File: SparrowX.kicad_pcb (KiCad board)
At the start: 4 copper layers, 31.6 x 26.6 mm, 31 parts, among them J1 NORTH, J2 SOUTH, J3 WEST, J4 EAST, U1 LMR43610MSC3RPERQ1, U2 LD49100PU33RY, U3 STM32G0B1CBU6, U4 TCAN332G, U5 TCAN332G

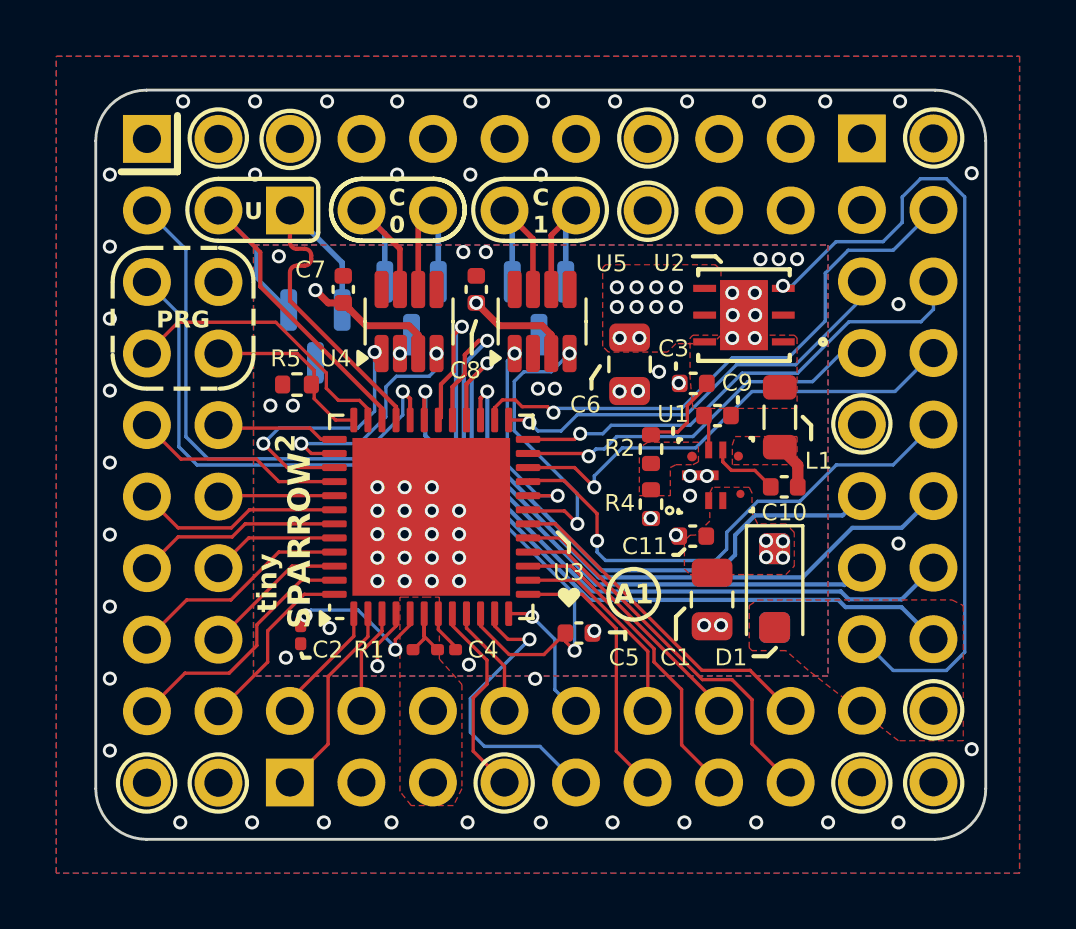
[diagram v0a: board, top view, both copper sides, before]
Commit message: DFM: get rid of 0201 SMD components
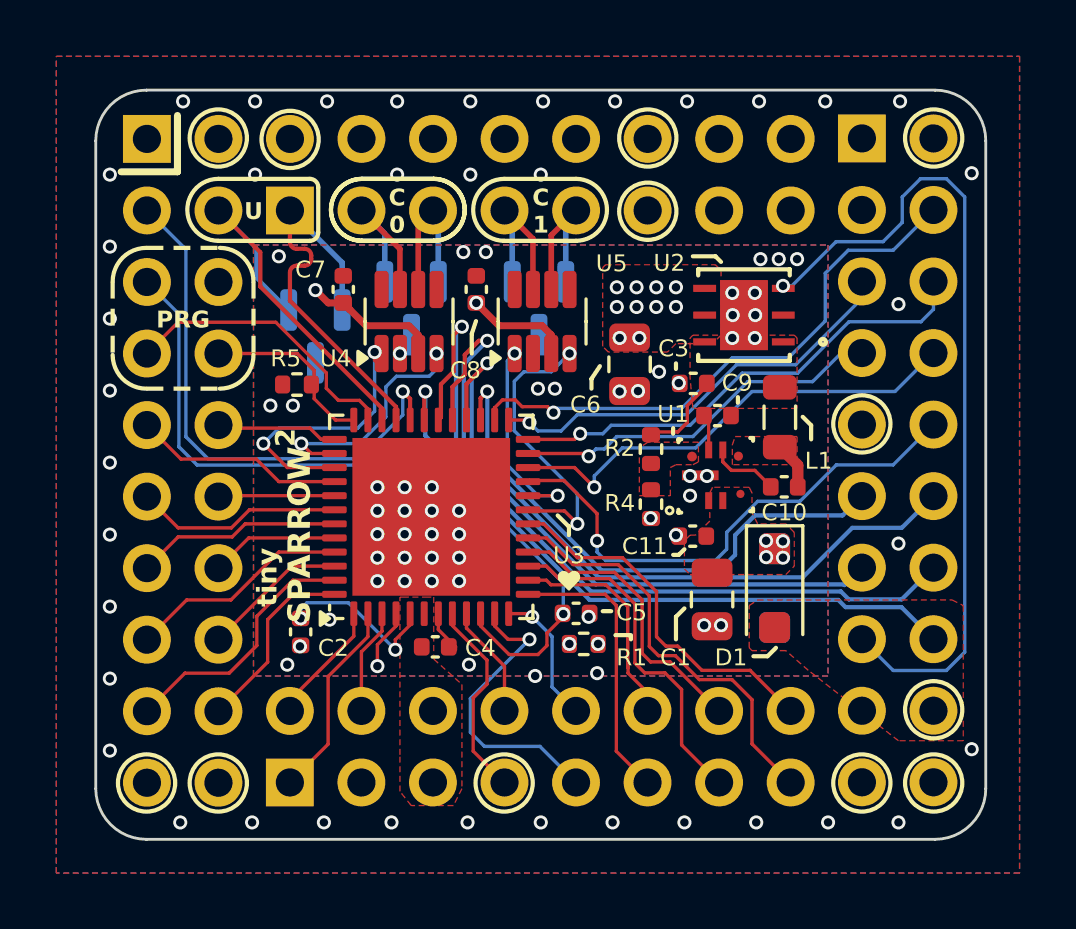
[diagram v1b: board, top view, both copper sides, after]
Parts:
- C1: value 4.7 uF -> 10 uF
- C2, C4: footprint Capacitor_SMD:C_0201_0603Metric -> Capacitor_SMD:C_0402_1005Metric
- R1: footprint Resistor_SMD:R_0201_0603Metric -> Resistor_SMD:R_0402_1005Metric
- moved R1 6.38 mm to (171.9, 100.5)
- moved C5 0.71 mm to (171.7, 99.4)
- moved G*** 0.60 mm to (171.4, 98.2)
- moved C4 0.41 mm to (166.7, 100.6)
- moved C2 0.10 mm to (161.9, 100.0)
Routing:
- net /VREF: track 5.83 -> 12.5 mm, vias 2 -> 3
- net +3V3: track 39.4 -> 36.5 mm, vias 12 -> 13
- net /~{RESET}: track 29.5 -> 27.8 mm
- net /PA6: track 13.8 -> 14.9 mm
- net /PA5: track 9.24 -> 10.2 mm
- net /PA4: track 11.4 -> 12.3 mm
- net /PA7: track 12.1 -> 13.0 mm
- net /PA3: track 7.42 -> 7.92 mm
- net GND: vias 91 -> 93
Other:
- board text removed: "A1"

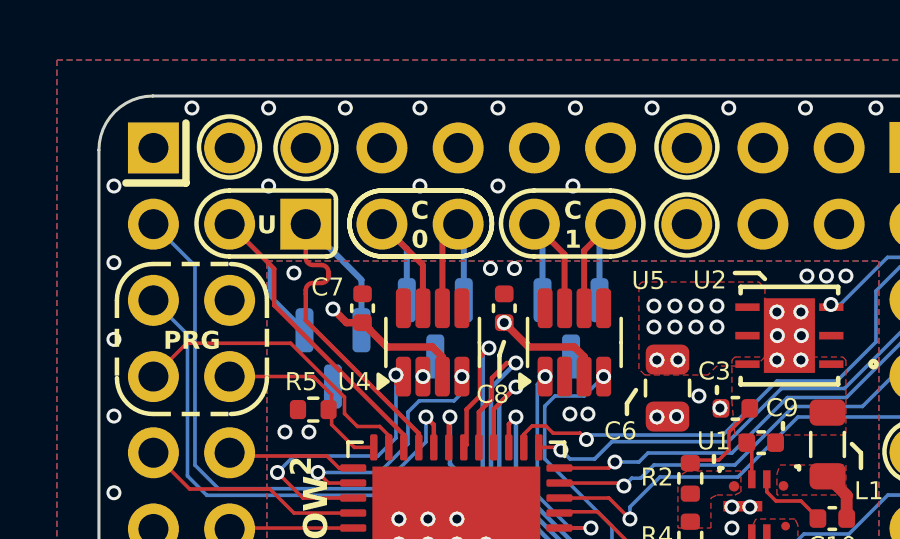
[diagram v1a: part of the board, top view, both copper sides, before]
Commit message: Silkscreen: fix 'double-C1' problem
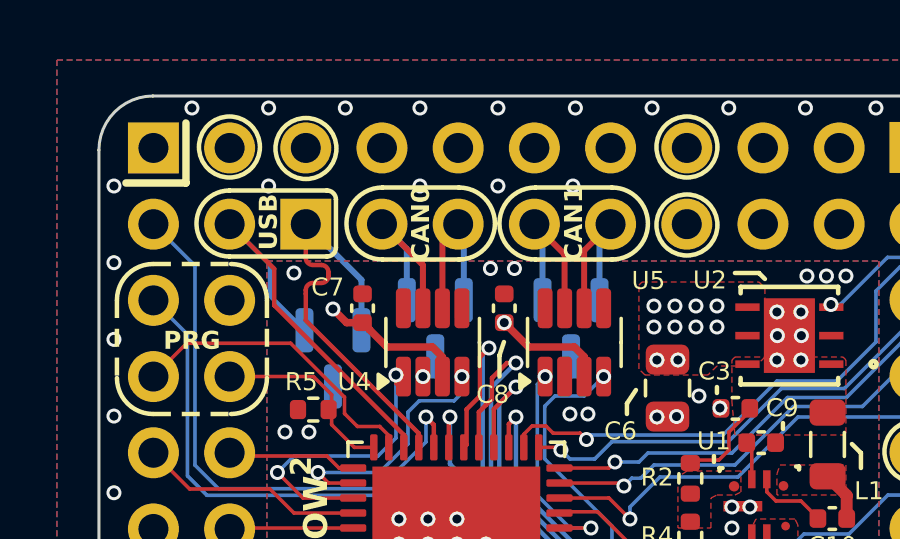
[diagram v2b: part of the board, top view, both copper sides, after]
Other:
- board text added: "CAN0"
- board text added: "CAN1"
- board text added: "USB"
- board text removed: "C 0"
- board text removed: "C 1"
- board text removed: "U"
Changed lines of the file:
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@@
+		(layer "B.SilkS")
+	)
+	(gr_line
+		(start 157.5 83.700002)
+		(end 155.5 83.700002)
+		(stroke
+			(width 0.25)
+			(type default)
+		)
 		(layer "B.SilkS")
 	)
@@
 	)
 	(gr_arc
-		(start 171.65 83.95)
-		(mid 172.75 85.05)
-		(end 171.65 86.15)
-		(stroke
-			(width 0.15)
-			(type default)
-		)
-		(layer "B.SilkS")
-	)
-	(gr_line
-		(start 169.1 83.95)
-		(end 171.65 83.95)
-		(stroke
-			(width 0.15)
-			(type default)
-		)
-		(layer "B.SilkS")
-	)
-	(gr_line
-		(start 169.1 86.15)
-		(end 171.65 86.15)
+		(start 164.05 86.25)
+		(mid 162.85 85.05)
+		(end 164.05 83.85)
 		(stroke
 			(width 0.15)
@@
 	)
 	(gr_line
-		(start 164.05 83.95)
-		(end 166.6 83.95)
-		(stroke
-			(width 0.15)
-			(type default)
-		)
-		(layer "B.SilkS")
-	)
-	(gr_arc
-		(start 166.6 83.95)
-		(mid 167.7 85.05)
-		(end 166.6 86.15)
+		(start 164.05 83.85)
+		(end 166.6 83.85)
 		(stroke
 			(width 0.15)
@@
 	)
 	(gr_line
-		(start 169.1 86.15)
-		(end 171.65 86.15)
-		(stroke
-			(width 0.15)
-			(type default)
-		)
-		(layer "B.SilkS")
-	)
-	(gr_arc
-		(start 169.1 86.15)
-		(mid 168 85.05)
-		(end 169.1 83.95)
-		(stroke
-			(width 0.15)
+		(start 169.15 83.85)
+		(end 171.7 83.85)
+		(stroke
+			(width 0.15)
+			(type default)
+		)
+		(layer "B.SilkS")
+	)
+	(gr_line
+		(start 157.5 81.700001)
+		(end 157.5 83.700002)
+		(stroke
+			(width 0.25)
 			(type default)
 		)
@@
 	)
 	(gr_arc
-		(start 171.65 83.95)
-		(mid 172.75 85.05)
-		(end 171.65 86.15)
+		(start 166.6 83.85)
+		(mid 167.8 85.05)
+		(end 166.6 86.25)
 		(stroke
 			(width 0.15)
@@
 	)
 	(gr_line
-		(start 164.05 86.15)
-		(end 166.6 86.15)
+		(start 169.15 86.25)
+		(end 171.7 86.25)
 		(stroke
 			(width 0.15)
@@
 		(layer "B.SilkS")
 	)
-	(gr_arc
-		(start 169.1 86.15)
-		(mid 168 85.05)
-		(end 169.1 83.95)
-		(stroke
-			(width 0.15)
-			(type default)
-		)
-		(layer "B.SilkS")
-	)
 	(gr_line
 		(start 167.5 90.15)
@@
 		(layer "B.SilkS")
 	)
-	(gr_line
-		(start 169.1 83.95)
-		(end 171.65 83.95)
-		(stroke
-			(width 0.15)
-			(type default)
-		)
-		(layer "B.SilkS")
-	)
-	(gr_arc
-		(start 164.05 86.15)
-		(mid 162.95 85.05)
-		(end 164.05 83.95)
+	(gr_arc
+		(start 169.15 86.25)
+		(mid 167.95 85.05)
+		(end 169.15 83.85)
 		(stroke
 			(width 0.15)
@@
 		(layer "B.SilkS")
 	)
+	(gr_line
+		(start 164.05 86.25)
+		(end 166.6 86.25)
+		(stroke
+			(width 0.15)
+			(type default)
+		)
+		(layer "B.SilkS")
+	)
 	(gr_circle
 		(center 169.1 105.4)
@@
 			(width 0.15)
 			(type dot)
+		)
+		(layer "B.SilkS")
+	)
+	(gr_arc
+		(start 171.7 83.85)
+		(mid 172.9 85.05)
+		(end 171.7 86.25)
+		(stroke
+			(width 0.15)
+			(type default)
 		)
 		(layer "B.SilkS")
@@
 		(layer "F.SilkS")
 	)
-	(gr_line
-		(start 166.6 86.15)
-		(end 164.05 86.15)
-		(stroke
-			(width 0.15)
-			(type default)
-		)
-		(layer "F.SilkS")
-	)
 	(gr_circle
 		(center 181.8 105.4)
@@
 		)
 		(fill none)
-		(layer "F.SilkS")
-	)
-	(gr_line
-		(start 171.65 86.15)
-		(end 169.1 86.15)
-		(stroke
-			(width 0.15)
-			(type default)
-		)
 		(layer "F.SilkS")
 	)
@@
 	)
 	(gr_arc
-		(start 171.65 83.95)
-		(mid 172.75 85.05)
-		(end 171.65 86.15)
-		(stroke
-			(width 0.15)
-			(type default)
-		)
-		(layer "F.SilkS")
-	)
-	(gr_line
-		(start 171.65 83.95)
-		(end 169.1 83.95)
-		(stroke
-			(width 0.15)
-			(type default)
-		)
-		(layer "F.SilkS")
-	)
-	(gr_arc
 		(start 160.200001 90.2)
 		(mid 159.848529 91.048528)
@@
 	)
 	(gr_arc
-		(start 164.05 86.15)
-		(mid 162.95 85.05)
-		(end 164.05 83.95)
+		(start 164.05 86.25)
+		(mid 162.85 85.05)
+		(end 164.05 83.85)
 		(stroke
 			(width 0.15)
@@
 		)
 		(fill none)
+		(layer "F.SilkS")
+	)
+	(gr_line
+		(start 171.7 86.25)
+		(end 169.15 86.25)
+		(stroke
+			(width 0.15)
+			(type default)
+		)
 		(layer "F.SilkS")
 	)
@@
 		(layer "F.SilkS")
 	)
-	(gr_arc
-		(start 164.05 86.15)
-		(mid 162.95 85.05)
-		(end 164.05 83.95)
-		(stroke
-			(width 0.15)
-			(type default)
-		)
-		(layer "F.SilkS")
-	)
 	(gr_circle
 		(center 158.95 105.4)
@@
 	)
 	(gr_arc
-		(start 166.6 83.95)
-		(mid 167.7 85.05)
-		(end 166.6 86.15)
+		(start 166.6 83.85)
+		(mid 167.8 85.05)
+		(end 166.6 86.25)
 		(stroke
 			(width 0.15)
@@
 		(layer "F.SilkS")
 	)
-	(gr_arc
-		(start 166.6 83.95)
-		(mid 167.7 85.05)
-		(end 166.6 86.15)
-		(stroke
-			(width 0.15)
-			(type default)
-		)
-		(layer "F.SilkS")
-	)
-	(gr_arc
-		(start 169.1 86.15)
-		(mid 168 85.05)
-		(end 169.1 83.95)
-		(stroke
-			(width 0.15)
-			(type default)
-		)
-		(layer "F.SilkS")
-	)
 	(gr_circle
 		(center 156.404 105.4)
@@
 	)
 	(gr_line
-		(start 166.6 83.95)
-		(end 164.05 83.95)
-		(stroke
-			(width 0.15)
-			(type default)
-		)
-		(layer "F.SilkS")
-	)
-	(gr_line
 		(start 162.2 86.15)
 		(end 158.95 86.15)
@@
 		(layer "F.SilkS")
 	)
+	(gr_arc
+		(start 171.7 83.85)
+		(mid 172.9 85.05)
+		(end 171.7 86.25)
+		(stroke
+			(width 0.15)
+			(type default)
+		)
+		(layer "F.SilkS")
+	)
+	(gr_arc
+		(start 169.15 86.25)
+		(mid 167.95 85.05)
+		(end 169.15 83.85)
+		(stroke
+			(width 0.15)
+			(type default)
+		)
+		(layer "F.SilkS")
+	)
 	(gr_line
 		(start 175.1 97.3)
@@
 		(layer "F.SilkS")
 	)
+	(gr_line
+		(start 171.7 83.85)
+		(end 169.15 83.85)
+		(stroke
+			(width 0.15)
+			(type default)
+		)
+		(layer "F.SilkS")
+	)
 	(gr_circle
 		(center 174.2 82.5)
@@
 	)
 	(gr_line
-		(start 166.6 86.15)
-		(end 164.05 86.15)
+		(start 166.6 86.25)
+		(end 164.05 86.25)
 		(stroke
 			(width 0.15)
@@
 	)
 	(gr_line
-		(start 166.6 83.95)
-		(end 164.05 83.95)
+		(start 166.6 83.85)
+		(end 164.05 83.85)
 		(stroke
 			(width 0.15)
@@
 		(layer "Edge.Cuts")
 	)
-	(gr_text "U"
-		(at 160.25 85.1 0)
+	(gr_text "CAN0"
+		(at 165.295 85.05 270)
 		(layer "B.SilkS")
 		(effects
@@
 		)
 	)
-	(gr_text "C\n0"
-		(at 165.3 85.1 0)
+	(gr_text "USB"
+		(at 160.2 85 -90)
 		(layer "B.SilkS")
 		(effects
@@
 		)
 	)
+	(gr_text "CAN1"
+		(at 170.365 85.04 270)
+		(layer "B.SilkS")
+		(effects
+			(font
+				(size 0.6 0.6)
+				(thickness 0.15)
+				(bold yes)
+			)
+			(justify mirror)
+		)
+	)
 	(gr_text "REV A1"
 		(at 166.45 99.6 0)
@@
 				)
 			)
-		)
-	)
-	(gr_text "C\n1"
-		(at 170.4 85.1 0)
-		(layer "B.SilkS")
-		(effects
-			(font
-				(size 0.6 0.6)
-				(thickness 0.15)
-				(bold yes)
-			)
-			(justify mirror)
 		)
 	)
@@
 		)
 	)
-	(gr_text "C\n1"
-		(at 170.4 85.1 0)
-		(layer "F.SilkS")
-		(effects
-			(font
-				(size 0.6 0.6)
-				(thickness 0.15)
-				(bold yes)
-			)
-		)
-	)
 	(gr_text "PRG"
 		(at 157.7 88.95 0)
@@
 		)
 	)
-	(gr_text "U"
-		(at 160.2 85.1 0)
+	(gr_text "CAN1"
+		(at 170.425 85.05 90)
 		(layer "F.SilkS")
 		(effects
@@
 		)
 	)
-	(gr_text "C\n0"
-		(at 165.3 85.1 0)
+	(gr_text "CAN0"
+		(at 165.325 85.05 90)
 		(layer "F.SilkS")
 		(effects
@@
 		)
 	)
+	(gr_text "USB"
+		(at 160.25 85 90)
+		(layer "F.SilkS")
+		(effects
+			(font
+				(size 0.6 0.6)
+				(thickness 0.15)
+				(bold yes)
+			)
+		)
+	)

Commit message: A2 revision
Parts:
- moved C8 5.02 mm to (171.6, 91.5), turned to 0 degrees
- moved C7 1.47 mm to (163.1, 89.3)
- moved D4 1.15 mm to (162.1, 88.4)
- moved R5 0.63 mm to (161.3, 91.7), turned to 90 degrees
- moved D2 0.32 mm to (165.6, 88.7)
- moved U4 0.26 mm to (165.5, 88.9)
- moved U5 0.07 mm to (170.4, 88.9)
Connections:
- J1 pad 2: VDC -> GND
- J3 pad 1: GND -> unconnected-(J3-Pin_1-Pad1)
- J3 pad 7: /SWDIO -> /SWCLK
- J3 pad 8: /SWCLK -> /SWDIO
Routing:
- net VDC: track 41.6 -> 0.00 mm
- net +3V3: track 36.5 -> 28.0 mm, vias 13 -> 11
- net /USB-: track 14.4 -> 11.0 mm, vias 0 -> 1
- net /USB+: track 14.4 -> 11.1 mm, vias 0 -> 1
- net /SWDIO: track 10.3 -> 7.24 mm, vias 0 -> 1
- net /SWCLK: track 6.37 -> 8.56 mm
- net /PA8: track 25.1 -> 27.2 mm
- net /PA9: track 24.2 -> 26.3 mm
- net /CAN0_RX: track 8.39 -> 10.1 mm
- net /PC6: track 27.9 -> 29.2 mm
- net GND: track 1.53 -> 2.71 mm, vias 93 -> 97
- net /CAN1_RX: track 10.3 -> 9.63 mm
- net /PB11: track 13.4 -> 13.9 mm
- net /CAN1-: track 5.71 -> 5.36 mm, vias 0 -> 1
- net /CAN1+: track 5.72 -> 5.37 mm, vias 0 -> 1
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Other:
- board text added: "REV A2"
- board text removed: "REV A1"

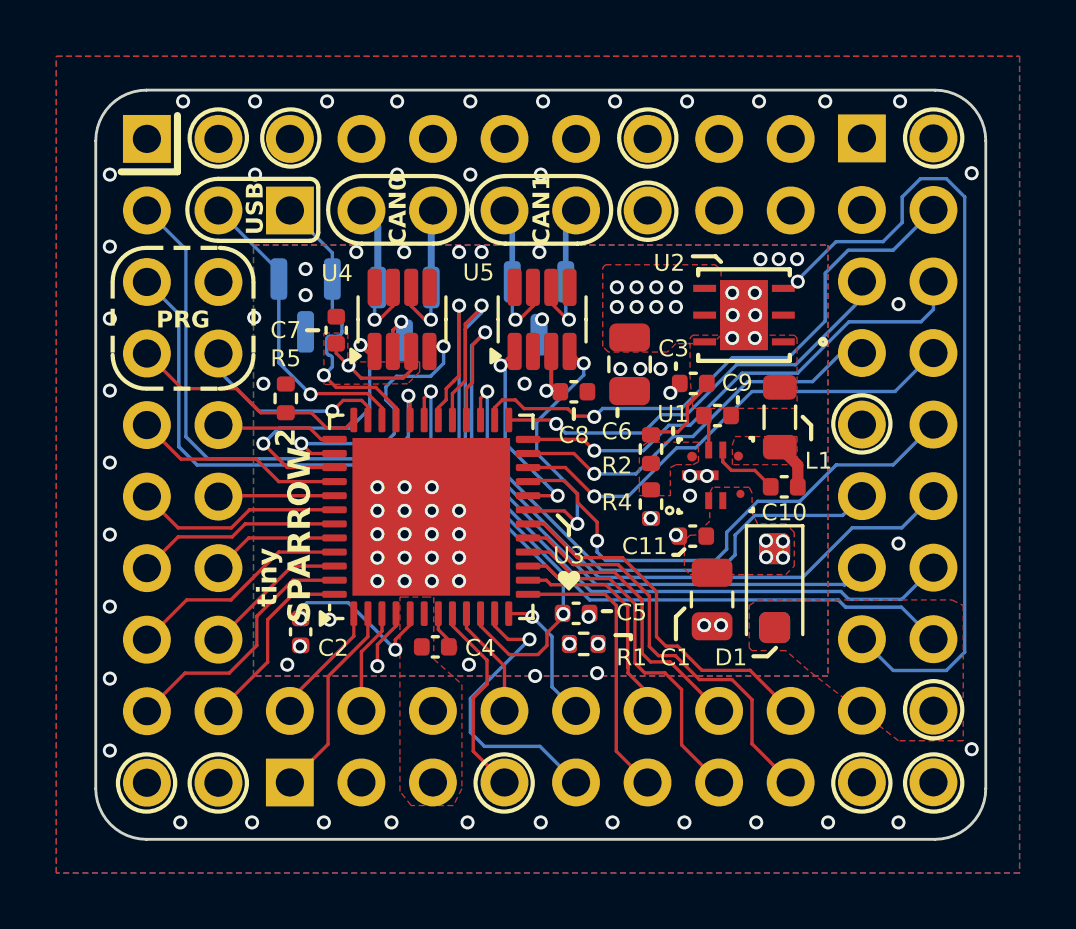
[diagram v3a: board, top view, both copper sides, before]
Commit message: Rev A2: add module corner key, silkscreen tweaks
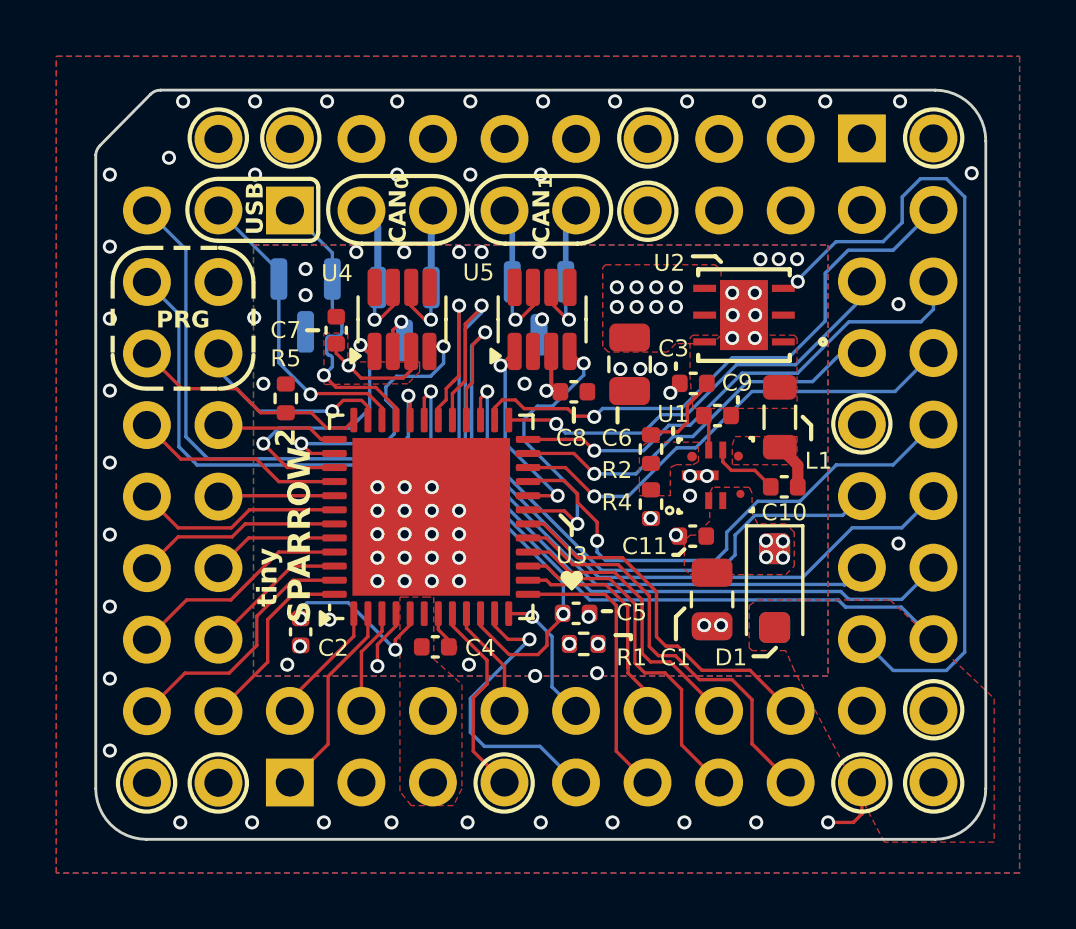
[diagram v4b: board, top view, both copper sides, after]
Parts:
- moved G*** 0.10 mm to (171.5, 98.2)
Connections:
- J4 pad 18: VDC -> GND
- J4 pad 20: GND -> VDC
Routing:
- net GND: track 2.71 -> 5.16 mm, vias 97 -> 96
- net /CAN1_RX: track 9.63 -> 10.3 mm
- removed copper zone on In2.Cu, net VDC
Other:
- outline, holes or cut-outs redrawn
- board text added: "CAN_{0}"
- board text added: "CAN_{1}"
- board text removed: "CAN0"
- board text removed: "CAN1"
